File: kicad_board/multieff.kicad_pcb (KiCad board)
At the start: 2 copper layers, 119 x 76 mm, 26 parts

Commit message: Latest pcb version
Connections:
- ADC1 pad 1: /3.3V -> +3.3V
- ADC1 pad 2: /GND -> GND
- ADC1 pad 3: /SDA -> /SCL
- ADC1 pad 4: /SCL -> /SDA
- ADC1 pad 5: /GND -> GND
- Joystick1 pad 1: /3.3V -> Net-(Joystick1-Pin_1)
- Joystick1 pad 4: Net-(Joystick1-Pin_4) -> +3.3V
- Joystick1 pad 5: /GND -> GND
- LED1 pad 1: /GND -> GND
- LED2 pad 1: /GND -> GND
- LED3 pad 1: /GND -> GND
- LED4 pad 1: /GND -> GND
- LEDAlim1 pad 1: /GND -> GND
- MCD1L1 pad 1: /3.3V -> +3.3V
- MCD1L1 pad 10: /GND -> GND
- MCD1L1 pad 2: /GND -> GND
- MCD1L1 pad 8: /GND -> GND
- MCD1L1 pad 9: /GND -> GND
- MCP1R1 pad 12: Net-(MCP1R1-Pin_12) -> Net-(Joystick1-Pin_1)
- MCP1R1 pad 20: Net-(Joystick1-Pin_4) -> unconnected-(MCP1R1-Pin_20-Pad20)
- MCP1R1 pad 9: unconnected-(MCP1R1-Pin_9-Pad9) -> Net-(MCP1R1-Pin_9)
- MCP2L1 pad 1: /3.3V -> +3.3V
- MCP2L1 pad 10: /GND -> GND
- MCP2L1 pad 2: /GND -> GND
- MCP2L1 pad 8: /3.3V -> +3.3V
- MCP2L1 pad 9: /GND -> GND
- PB1 pad 1: /GND -> GND
- PB2 pad 1: /GND -> GND
- PB3 pad 1: /GND -> GND
- PB4 pad 1: /GND -> GND
- Pisound1 pad 1: /5V -> GND
- Pisound1 pad 13: /SCL -> /SDA
- Pisound1 pad 14: /SDA -> /SCL
- Pisound1 pad 2: /GND -> /5V
- Pisound1 pad 3: /3.3V -> unconnected-(Pisound1-Pin_3-Pad3)
- Pisound1 pad 4: unconnected-(Pisound1-Pin_4-Pad4) -> +3.3V
- RE1 pad 1: /GND -> GND
- RE1 pad 2: /3.3V -> +3.3V
- RE1 pad 3: Net-(MCP1R1-Pin_15) -> Net-(MCP1R1-Pin_13)
- RE1 pad 4: Net-(MCP1R1-Pin_13) -> Net-(MCP1R1-Pin_11)
- RE1 pad 5: Net-(MCP1R1-Pin_11) -> Net-(MCP1R1-Pin_9)
- RE2 pad 1: /GND -> GND
- RE2 pad 2: /3.3V -> +3.3V
- RE2 pad 3: Net-(MCP1R1-Pin_12) -> Net-(MCP1R1-Pin_14)
- RE2 pad 4: Net-(MCP1R1-Pin_14) -> Net-(MCP1R1-Pin_16)
- RE2 pad 5: Net-(MCP1R1-Pin_16) -> Net-(MCP1R1-Pin_15)
- RE3 pad 1: /GND -> GND
- RE3 pad 2: /3.3V -> +3.3V
- RE4 pad 1: /GND -> GND
- RE4 pad 2: /3.3V -> +3.3V
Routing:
- net GND: track 0.00 -> 508.3 mm
- net /GND: track 435.3 -> 0.00 mm
- net +3.3V: track 0.00 -> 229.7 mm
- net /3.3V: track 209.1 -> 0.00 mm
- net Net-(Joystick1-Pin_1): track 0.00 -> 48.0 mm
- net Net-(Joystick1-Pin_4): track 35.3 -> 0.00 mm
- net Net-(MCP1R1-Pin_9): track 0.00 -> 33.9 mm
- net Net-(MCP1R1-Pin_12): track 26.6 -> 0.00 mm
- net Net-(MCP2R1-Pin_12): track 38.9 -> 35.4 mm
- net Net-(MCP2R1-Pin_10): track 39.9 -> 37.0 mm
- net /SDA: track 80.6 -> 77.9 mm
- net Net-(MCP1R1-Pin_15): track 19.3 -> 21.7 mm
- net Net-(MCP2R1-Pin_8): track 40.2 -> 38.2 mm
- net Net-(MCP1R1-Pin_14): track 22.6 -> 24.1 mm
- net /SCL: track 76.5 -> 77.9 mm
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
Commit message: Add connector for expression pedal
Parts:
- added WHA1: Conn_01x02, Connector_Wire:SolderWire-0.1sqmm_1x02_P3.6mm_D0.4mm_OD1mm, F.Cu at (50.4, 81.0)
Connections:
- MCP1R1 pad 17: unconnected-(MCP1R1-Pin_17-Pad17) -> Net-(MCP1R1-Pin_17)
- MCP1R1 pad 18: unconnected-(MCP1R1-Pin_18-Pad18) -> Net-(MCP1R1-Pin_18)
- MCP2R1 pad 17: unconnected-(MCP2R1-Pin_17-Pad17) -> Net-(MCP2R1-Pin_17)
- MCP2R1 pad 18: unconnected-(MCP2R1-Pin_18-Pad18) -> Net-(MCP2R1-Pin_18)
- Pisound1 pad 3: unconnected-(Pisound1-Pin_3-Pad3) -> Net-(MCP2R1-Pin_17)
- Pisound1 pad 5: unconnected-(Pisound1-Pin_5-Pad5) -> Net-(MCP2R1-Pin_18)
- Pisound1 pad 7: unconnected-(Pisound1-Pin_7-Pad7) -> Net-(MCP1R1-Pin_17)
- Pisound1 pad 9: unconnected-(Pisound1-Pin_9-Pad9) -> Net-(MCP1R1-Pin_18)
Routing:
- net Net-(MCP1R1-Pin_17): track 0.00 -> 130.4 mm
- net Net-(MCP2R1-Pin_17): track 0.00 -> 128.8 mm
- net Net-(MCP2R1-Pin_18): track 0.00 -> 107.8 mm
- net Net-(MCP1R1-Pin_18): track 0.00 -> 103.4 mm
- net unconnected-(ADC1-Pin_6-Pad6): track 0.00 -> 12.7 mm

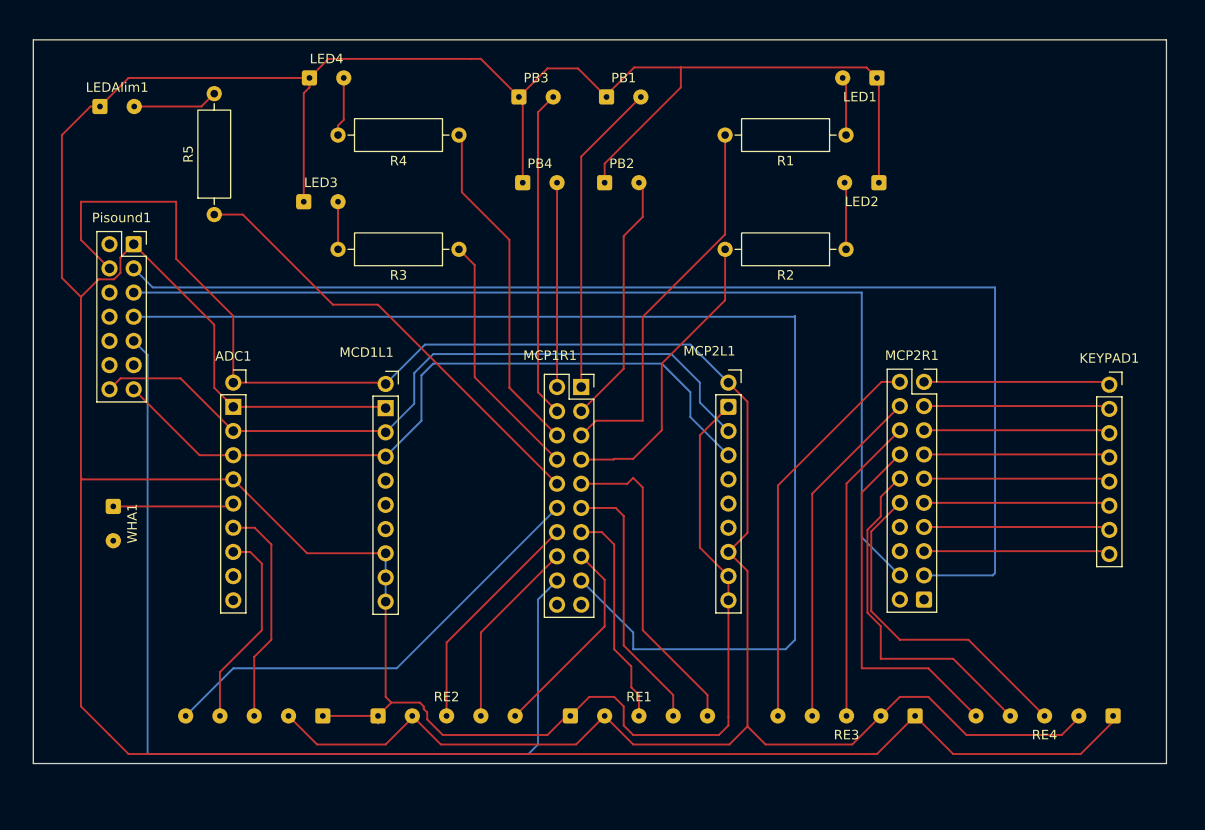
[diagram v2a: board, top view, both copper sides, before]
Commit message: With zones and jst connectors
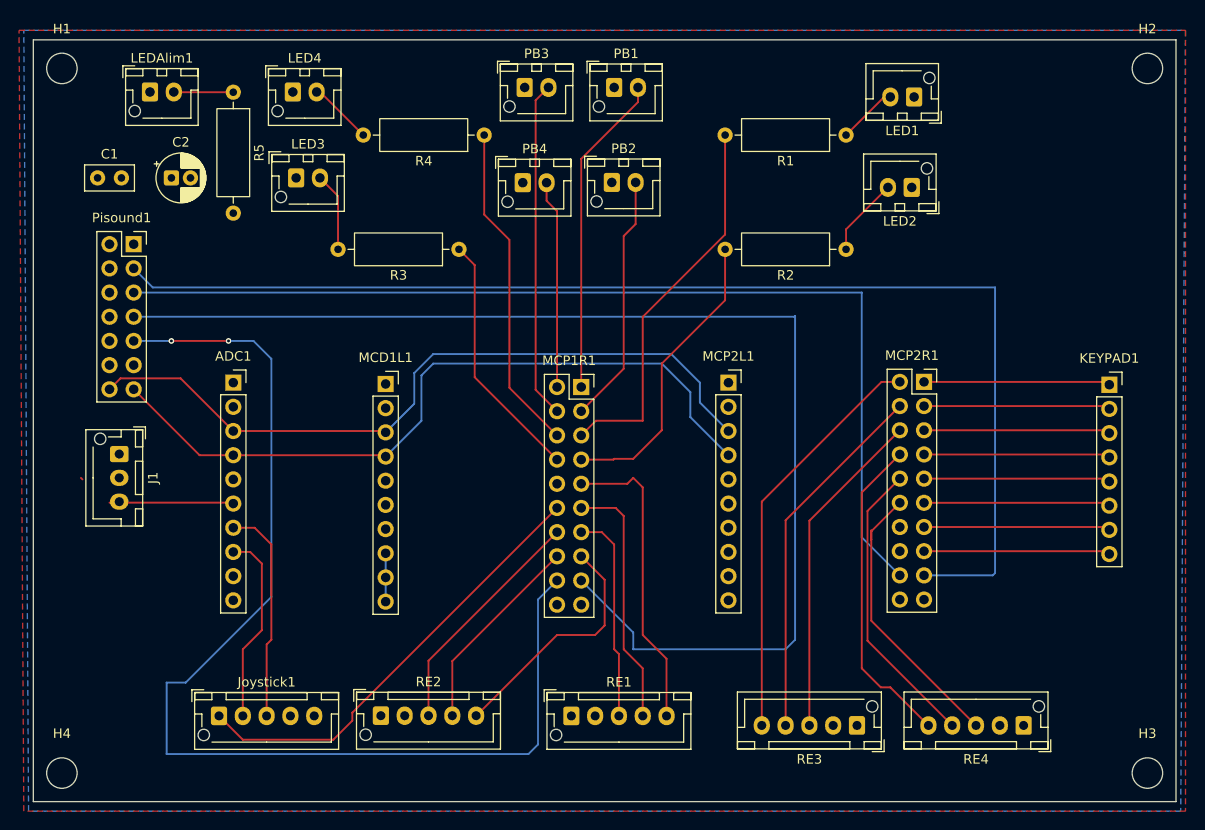
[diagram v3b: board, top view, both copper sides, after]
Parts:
- removed WHA1: Conn_01x02, Connector_Wire:SolderWire-0.1sqmm_1x02_P3.6mm_D0.4mm_OD1mm
- added C1: C, Capacitor_THT:C_Disc_D5.0mm_W2.5mm_P2.50mm, F.Cu at (48.8, 46.5)
- added C2: C_Polarized, Capacitor_THT:CP_Radial_D5.0mm_P2.00mm, F.Cu at (56.5, 46.5)
- added H1: MountingHole, MountingHole:MountingHole_3.2mm_M3, F.Cu at (45.0, 35.0)
- added H2: MountingHole, MountingHole:MountingHole_3.2mm_M3, F.Cu at (159.0, 35.0)
- added H3: MountingHole, MountingHole:MountingHole_3.2mm_M3, F.Cu at (159.0, 109.0)
- added H4: MountingHole, MountingHole:MountingHole_3.2mm_M3, F.Cu at (45.0, 109.0)
- added J1: Wha1, Connector_JST:JST_XH_B3B-XH-AM_1x03_P2.50mm_Vertical, F.Cu at (51.0, 75.5)
- Joystick1, RE1, RE2, RE3, RE4: footprint Connector_Wire:SolderWire-0.1sqmm_1x05_P3.6mm_D0.4mm_OD1mm -> Connector_JST:JST_XH_B5B-XH-AM_1x05_P2.50mm_Vertical
- LED1, LED2, LED3, LED4, LEDAlim1, PB1, PB2, PB3, PB4: footprint Connector_Wire:SolderWire-0.1sqmm_1x02_P3.6mm_D0.4mm_OD1mm -> Connector_JST:JST_XH_B2B-XH-AM_1x02_P2.50mm_Vertical
- moved R5 13.0 mm to (63.0, 37.5), turned to -90 degrees
- moved RE4 9.45 mm to (146.0, 104.0)
- moved RE3 6.18 mm to (128.5, 104.0)
- moved LEDAlim1 5.47 mm to (54.2, 37.5)
- moved LED1 4.38 mm to (134.5, 38.0)
- moved Joystick1 3.50 mm to (61.5, 103.0)
- moved LED2 3.49 mm to (134.2, 47.5)
- moved R4 2.65 mm to (89.3, 42.0)
- moved LED3 2.62 mm to (69.6, 46.5)
- moved LED4 2.29 mm to (69.2, 37.5)
- moved PB1 1.28 mm to (103.0, 37.0)
- moved PB3 1.17 mm to (93.6, 37.0)
- moved PB2 0.75 mm to (102.8, 47.0)
- moved RE2 0.30 mm to (78.5, 103.0)
- moved RE1 0.10 mm to (98.5, 103.0)
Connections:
- ADC1 pad 6: unconnected-(ADC1-Pin_6-Pad6) -> Net-(ADC1-Pin_6)
- MCP1R1 pad 10: Net-(MCP1R1-Pin_10) -> unconnected-(MCP1R1-Pin_10-Pad10)
- R5 pad 1: Net-(MCP1R1-Pin_10) -> Net-(LEDAlim1-Pin_2)
- R5 pad 2: Net-(LEDAlim1-Pin_2) -> +3.3V
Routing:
- net GND: track 508.3 -> 5.31 mm
- net +3.3V: track 229.7 -> 0.00 mm
- net Net-(MCP1R1-Pin_10): track 47.7 -> 0.00 mm
- net Net-(MCP1R1-Pin_18): track 103.4 -> 119.9 mm, vias 0 -> 2
- net Net-(ADC1-Pin_6): track 0.00 -> 13.0 mm
- net unconnected-(ADC1-Pin_6-Pad6): track 12.7 -> 0.00 mm
- net Net-(MCP2R1-Pin_10): track 37.0 -> 31.0 mm
- net Net-(MCP2R1-Pin_12): track 35.4 -> 30.2 mm
- net Net-(MCP2R1-Pin_8): track 38.2 -> 33.6 mm
- net Net-(MCP1R1-Pin_15): track 21.7 -> 25.7 mm
- net Net-(LED3-Pin_2): track 5.00 -> 8.29 mm
- net Net-(LEDAlim1-Pin_2): track 8.96 -> 6.26 mm
- net Net-(MCP2R1-Pin_6): track 32.3 -> 34.9 mm
- net Net-(MCP2R1-Pin_4): track 36.4 -> 38.5 mm
- net Net-(MCP1R1-Pin_9): track 33.9 -> 32.2 mm
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- added copper zone on B.Cu, net +3.3V
- added copper zone on F.Cu, net GND
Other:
- board size 119 x 76 mm -> 120 x 80 mm
